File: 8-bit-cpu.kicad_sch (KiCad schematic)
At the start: 24 parts

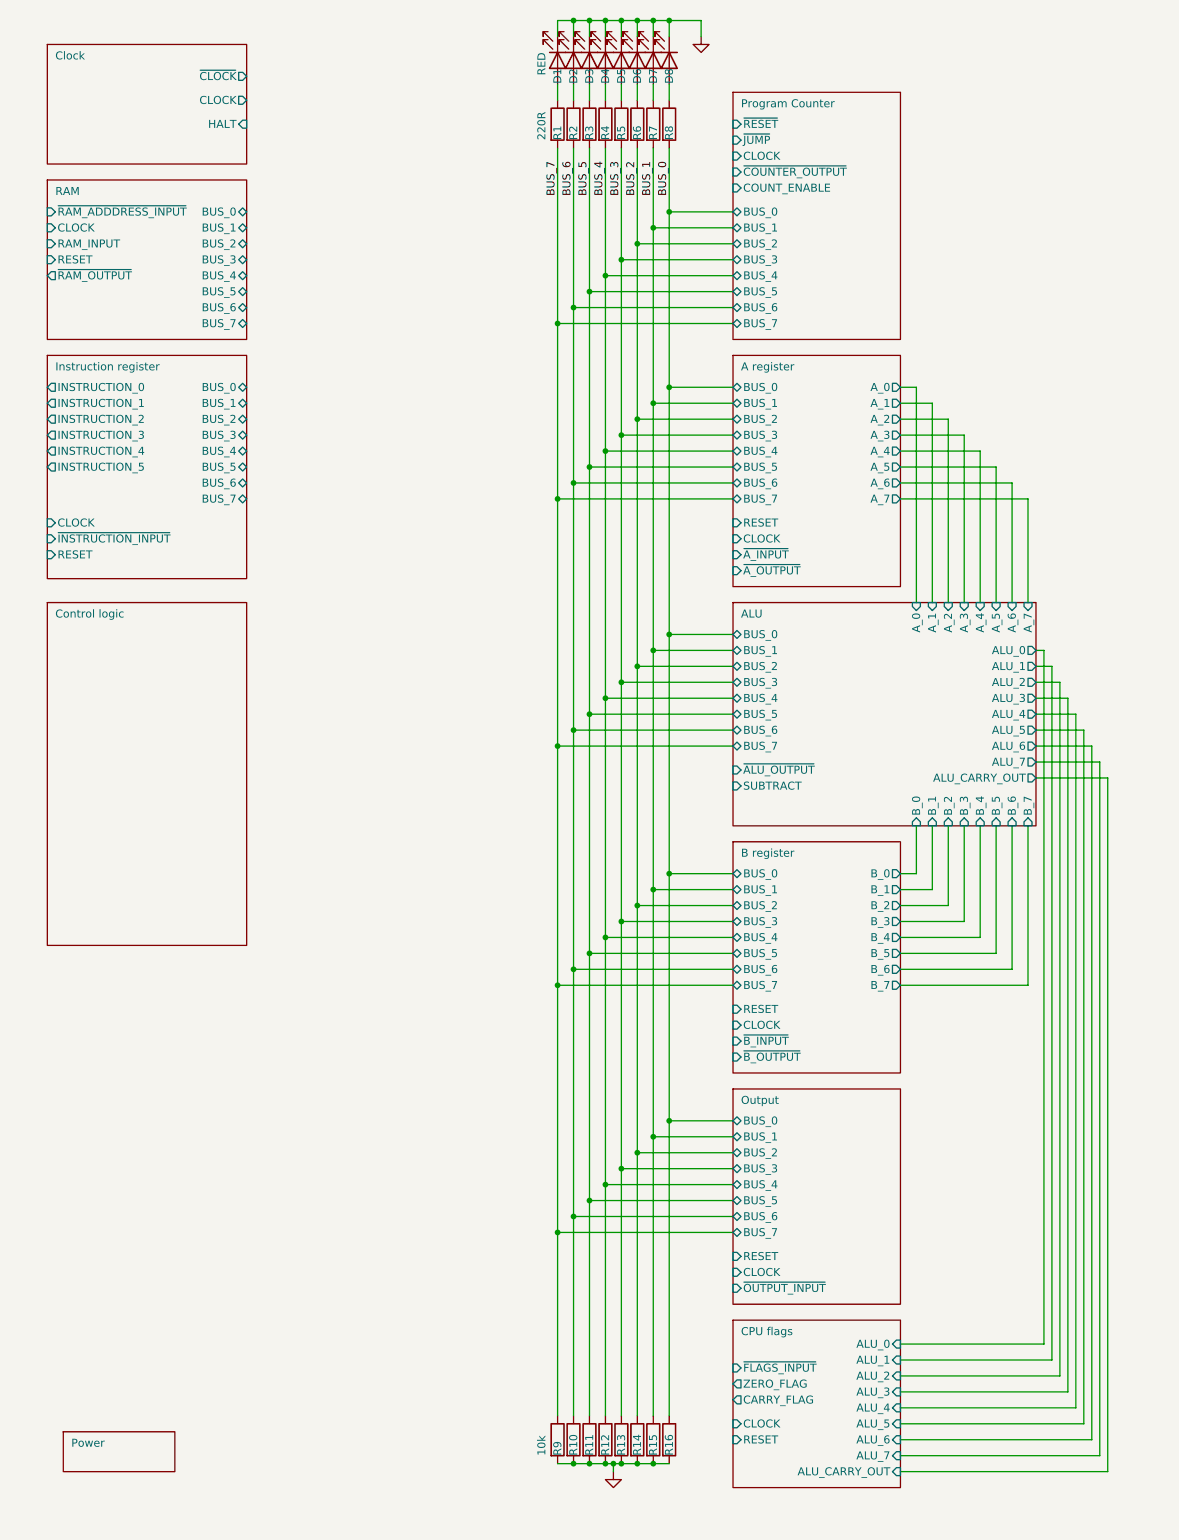
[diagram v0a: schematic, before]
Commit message: finished the control logic
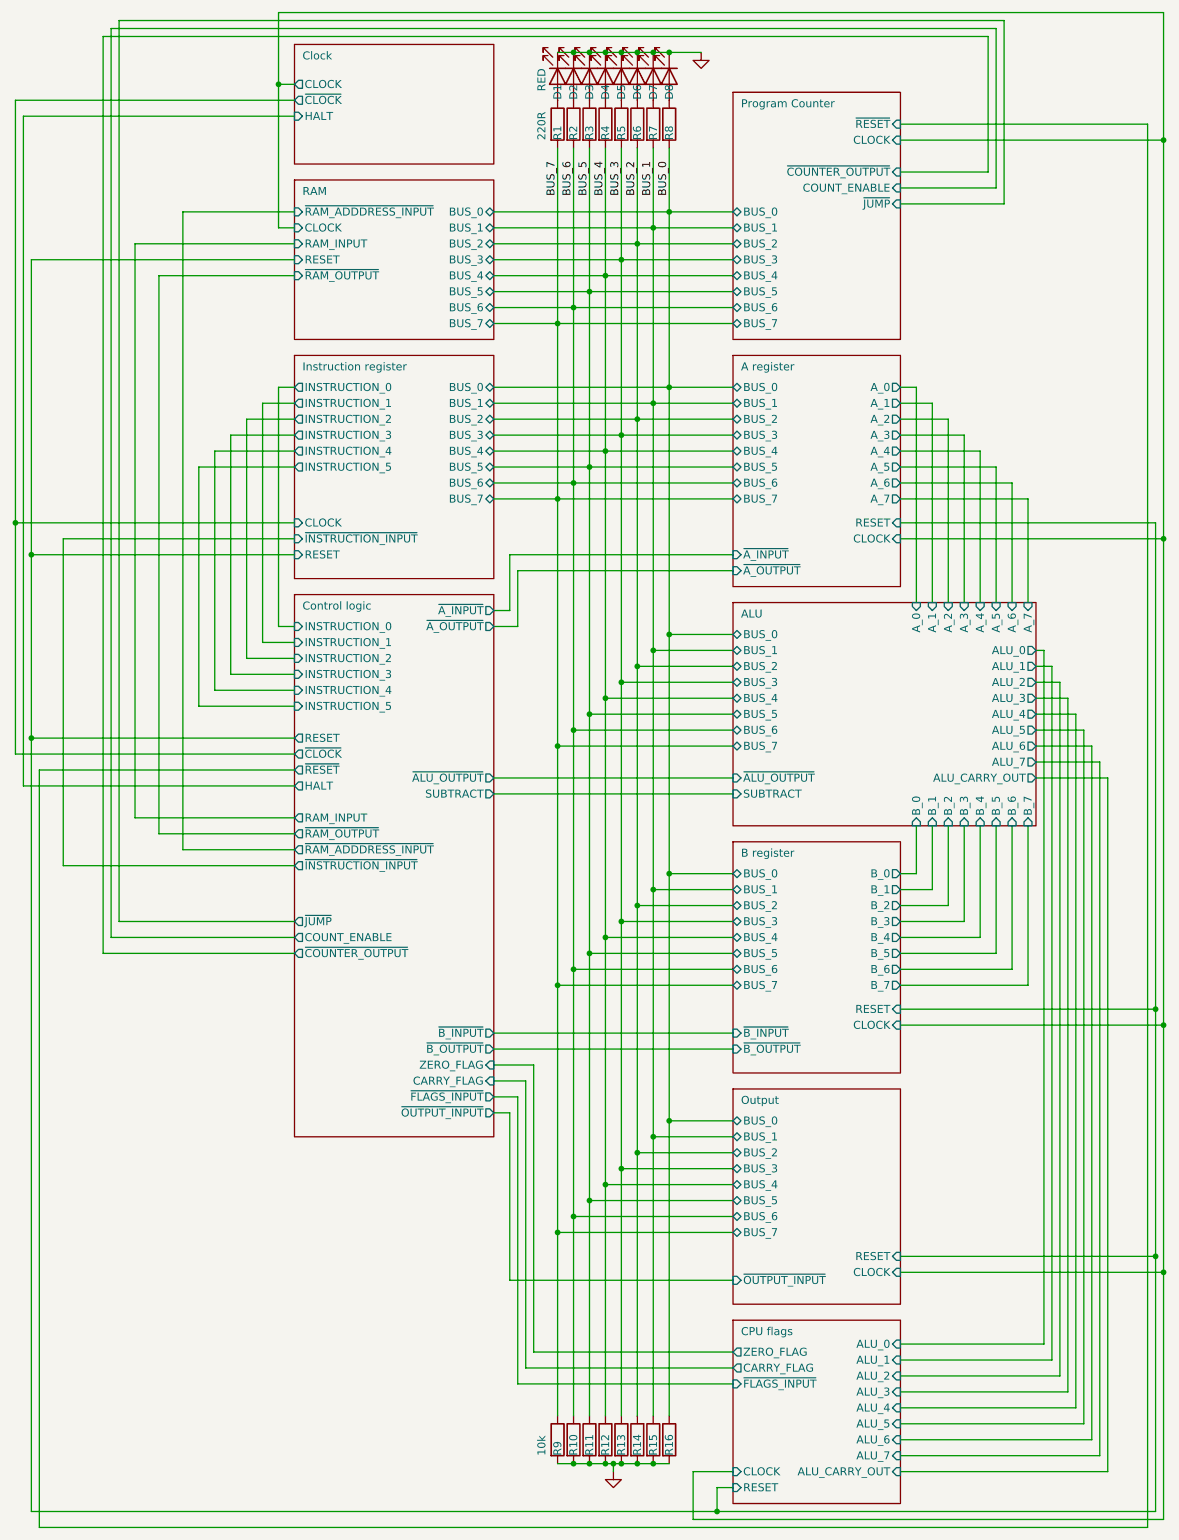
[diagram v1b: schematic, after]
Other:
- removed sheet Power
- sheet Control logic ports: added CARRY_FLAG, COUNT_ENABLE, HALT, INSTRUCTION_0, INSTRUCTION_1, INSTRUCTION_2, INSTRUCTION_3, INSTRUCTION_4, INSTRUCTION_5, RAM_INPUT, RESET, SUBTRACT, ZERO_FLAG, ~{ALU_OUTPUT}, ~{A_INPUT}, ~{A_OUTPUT}, ~{B_INPUT}, ~{B_OUTPUT}, ~{CLOCK}, ~{COUNTER_OUTPUT}, ~{FLAGS_INPUT}, ~{INSTRUCTION_INPUT}, ~{JUMP}, ~{OUTPUT_INPUT}, ~{RAM_ADDDRESS_INPUT}, ~{RAM_OUTPUT}, ~{RESET}; removed none
- moved on the sheet: D1, D2, D3, D4, D5, D6, D7, D8
